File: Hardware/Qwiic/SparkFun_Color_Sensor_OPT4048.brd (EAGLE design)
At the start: 25.4 x 25.4 mm, 53 parts, among them J1 QWIIC_RIGHT_ANGLE, J2 QWIIC_RIGHT_ANGLE, U1 OPT4048

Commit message: Rolls version
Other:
- board text added: "v10"
- board text removed: "v01"
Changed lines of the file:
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@@
 <drawing>
 <settings>
-<setting alwaysvectorfont="no"/>
+<setting alwaysvectorfont="yes"/>
 <setting keepoldvectorfont="yes"/>
 <setting verticaltext="up"/>
@@
 <layer number="45" name="Holes" color="7" fill="1" visible="yes" active="yes"/>
 <layer number="46" name="Milling" color="3" fill="1" visible="no" active="yes"/>
-<layer number="47" name="Measures" color="7" fill="1" visible="no" active="yes"/>
+<layer number="47" name="Measures" color="7" fill="1" visible="yes" active="yes"/>
 <layer number="48" name="Document" color="7" fill="1" visible="no" active="yes"/>
 <layer number="49" name="Reference" color="13" fill="1" visible="yes" active="yes"/>
@@
 <wire x1="0" y1="0" x2="25.4" y2="0" width="0.2032" layer="20"/>
 <wire x1="25.4" y1="0" x2="25.4" y2="25.4" width="0.2032" layer="20"/>
-<text x="24.139525" y="11.420475" size="0.8128" layer="16" font="vector" ratio="22" rot="MR90">v01</text>
+<text x="24.139525" y="11.420475" size="0.8128" layer="16" font="vector" ratio="22" rot="MR90">v10</text>
 <text x="31.75" y="25.4" size="1.778" layer="51" font="vector">1.6mm Thickness
 1 oz. Copper
@@
 </signals>
 <mfgpreviewcolors>
-<mfgpreviewcolor name="soldermaskcolor" color="0xC8AA0000"/>
+<mfgpreviewcolor name="soldermaskcolor" color="0xC8000000"/>
 <mfgpreviewcolor name="silkscreencolor" color="0xFFFEFEFE"/>
-<mfgpreviewcolor name="backgroundcolor" color="0xFF282828"/>
+<mfgpreviewcolor name="backgroundcolor" color="0xFFFFFFFF"/>
 <mfgpreviewcolor name="coppercolor" color="0xFFFFBF00"/>
 <mfgpreviewcolor name="substratecolor" color="0xFF786E46"/>

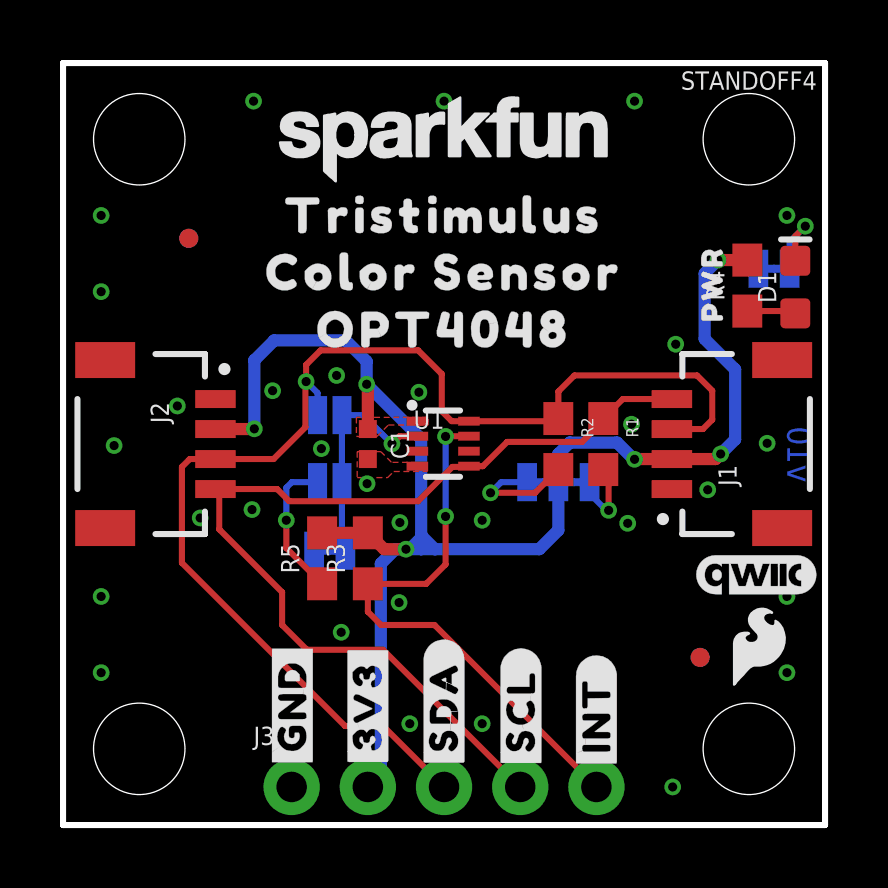
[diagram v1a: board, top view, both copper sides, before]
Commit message: Adds jumper to interrupt pin on both designs
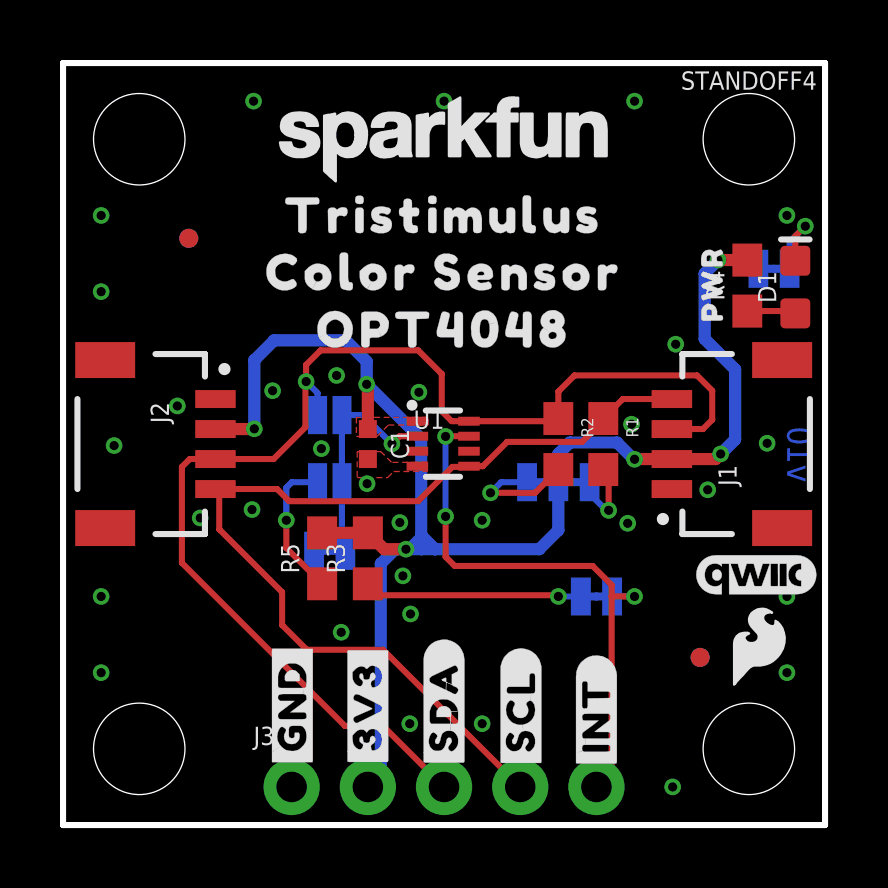
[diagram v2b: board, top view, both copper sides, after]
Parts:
- added INT: JUMPER-SMT_2_NC_TRACE_SILK, SparkFun-Jumpers:SMT-JUMPER_2_NC_TRACE_SILK
- added U$23: (no value), top:#INT#9
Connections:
- new net N$1: INT.2, R3.1
- net INT: now also INT.1; no longer R3.1
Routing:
- net N$1: track 0.00 -> 7.27 mm, vias 0 -> 1
- net INT: track 18.9 -> 19.2 mm, vias 2 -> 3
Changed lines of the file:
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@@
 <drawing>
 <settings>
-<setting alwaysvectorfont="yes"/>
+<setting alwaysvectorfont="no"/>
 <setting keepoldvectorfont="yes"/>
 <setting verticaltext="up"/>
@@
 <layer number="45" name="Holes" color="7" fill="1" visible="yes" active="yes"/>
 <layer number="46" name="Milling" color="3" fill="1" visible="no" active="yes"/>
-<layer number="47" name="Measures" color="7" fill="1" visible="yes" active="yes"/>
+<layer number="47" name="Measures" color="7" fill="1" visible="no" active="yes"/>
 <layer number="48" name="Document" color="7" fill="1" visible="no" active="yes"/>
 <layer number="49" name="Reference" color="13" fill="1" visible="yes" active="yes"/>
@@
 <element name="U$11" library="top" package="#0X45#18" value="" x="5.6896" y="11.4046" smashed="yes" rot="MR0"/>
 <element name="U$21" library="top" package="#0X46#18" value="" x="5.6388" y="13.589" smashed="yes" rot="MR0"/>
+<element name="INT" library="SparkFun-Jumpers" package="SMT-JUMPER_2_NC_TRACE_SILK" package3d_urn="urn:adsk.eagle:package:39281/1" value="JUMPER-SMT_2_NC_TRACE_SILK" x="17.78" y="7.62" smashed="yes" rot="MR0">
+<attribute name="NAME" x="17.78" y="8.763" size="0.6096" layer="26" font="vector" ratio="20" rot="MR0" align="bottom-center"/>
+<attribute name="VALUE" x="17.78" y="6.477" size="0.6096" layer="28" font="vector" ratio="20" rot="MR0" align="top-center"/>
+</element>
+<element name="U$23" library="top" package="#INT#9" value="" x="14.986" y="7.62" smashed="yes" rot="MR0"/>
 </elements>
 <signals>
@@
 <contactref element="J3" pad="1"/>
 <via x="11.2268" y="10.0838" extent="1-16" drill="0.3048"/>
-<via x="11.2014" y="7.4168" extent="1-16" drill="0.3048"/>
+<via x="11.5824" y="7.0358" extent="1-16" drill="0.3048"/>
 <via x="11.557" y="3.3782" extent="1-16" drill="0.3048"/>
 <via x="9.271" y="6.4262" extent="1-16" drill="0.3048"/>
@@
 <via x="9.1186" y="14.986" extent="1-16" drill="0.3048"/>
 <via x="8.6106" y="12.5476" extent="1-16" drill="0.3048"/>
+<via x="11.3284" y="8.3058" extent="1-16" drill="0.3048"/>
 </signal>
 <signal name="SCL">
@@
 <signal name="INT">
 <contactref element="U1" pad="P7"/>
-<contactref element="R3" pad="1"/>
 <wire x1="13.531" y1="12.962" x2="12.7588" y2="12.962" width="0.2032" layer="1"/>
 <wire x1="12.7588" y1="12.962" x2="12.7508" y2="12.954" width="0.2032" layer="1"/>
@@
 <wire x1="12.7508" y1="12.954" x2="12.7508" y2="10.287" width="0.2032" layer="16"/>
 <via x="12.7508" y="10.287" extent="1-16" drill="0.3048"/>
-<wire x1="10.16" y1="8.04" x2="12.104" y2="8.04" width="0.2032" layer="1"/>
-<wire x1="12.7508" y1="8.6868" x2="12.7508" y2="10.287" width="0.2032" layer="1"/>
-<wire x1="12.104" y1="8.04" x2="12.7508" y2="8.6868" width="0.2032" layer="1"/>
 <contactref element="J3" pad="5"/>
-<wire x1="17.78" y1="1.27" x2="12.381815625" y2="6.668184375" width="0.2032" layer="1"/>
-<wire x1="12.381815625" y1="6.668184375" x2="11.494184375" y2="6.668184375" width="0.2032" layer="1"/>
-<wire x1="11.494184375" y1="6.668184375" x2="10.603815625" y2="6.668184375" width="0.2032" layer="1"/>
-<wire x1="10.603815625" y1="6.668184375" x2="10.16" y2="7.112" width="0.2032" layer="1"/>
-<wire x1="10.16" y1="7.112" x2="10.16" y2="8.04" width="0.2032" layer="1"/>
+<contactref element="INT" pad="1"/>
+<wire x1="12.7508" y1="10.287" x2="12.7508" y2="8.9408" width="0.2032" layer="1"/>
+<wire x1="12.7508" y1="8.9408" x2="13.0556" y2="8.636" width="0.2032" layer="1"/>
+<wire x1="17.653" y1="8.636" x2="18.288" y2="8.001" width="0.2032" layer="1"/>
+<wire x1="18.288" y1="8.001" x2="18.288" y2="7.62" width="0.2032" layer="1"/>
+<wire x1="18.288" y1="7.62" x2="18.288" y2="1.778" width="0.2032" layer="1"/>
+<wire x1="18.288" y1="1.778" x2="17.78" y2="1.27" width="0.2032" layer="1"/>
+<wire x1="13.0556" y1="8.636" x2="17.653" y2="8.636" width="0.2032" layer="1"/>
+<wire x1="18.288" y1="7.62" x2="19.05" y2="7.62" width="0.2032" layer="1"/>
+<via x="19.05" y="7.62" extent="1-16" drill="0.3048"/>
+<wire x1="19.05" y1="7.62" x2="18.3007" y2="7.62" width="0.2032" layer="16"/>
 </signal>
 <signal name="3.3V">
@@
 <via x="7.4422" y="10.16" extent="1-16" drill="0.3048"/>
 </signal>
+<signal name="N$1">
+<contactref element="INT" pad="2"/>
+<contactref element="R3" pad="1"/>
+<wire x1="10.16" y1="8.04" x2="10.541" y2="7.659" width="0.2032" layer="1"/>
+<wire x1="16.471" y1="7.659" x2="10.541" y2="7.659" width="0.2032" layer="1"/>
+<wire x1="16.471" y1="7.659" x2="16.51" y2="7.62" width="0.2032" layer="1"/>
+<via x="16.51" y="7.62" extent="1-16" drill="0.3048"/>
+<wire x1="16.51" y1="7.62" x2="17.2593" y2="7.62" width="0.2032" layer="16"/>
+</signal>
 </signals>

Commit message: Revert "Adds jumper to interrupt pin on both designs"
This reverts commit a39334068ad88ec2875ce3e39fad74091b9d5839.
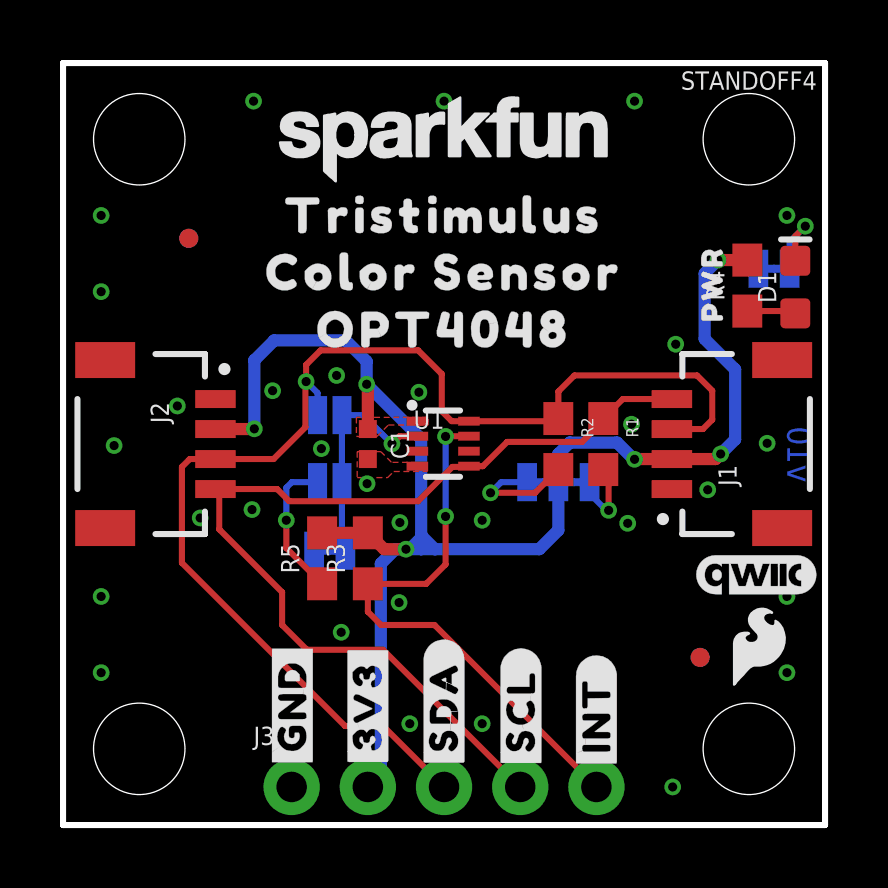
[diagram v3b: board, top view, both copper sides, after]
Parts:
- removed INT: JUMPER-SMT_2_NC_TRACE_SILK, SparkFun-Jumpers:SMT-JUMPER_2_NC_TRACE_SILK
- removed U$23: (no value), top:#INT#9
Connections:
- removed net N$1: INT.2, R3.1
- net INT: now also R3.1; no longer INT.1
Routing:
- net N$1: track 7.27 -> 0.00 mm, vias 1 -> 0
- net INT: track 19.2 -> 18.9 mm, vias 3 -> 2
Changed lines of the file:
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@@
 <drawing>
 <settings>
-<setting alwaysvectorfont="no"/>
+<setting alwaysvectorfont="yes"/>
 <setting keepoldvectorfont="yes"/>
 <setting verticaltext="up"/>
@@
 <layer number="45" name="Holes" color="7" fill="1" visible="yes" active="yes"/>
 <layer number="46" name="Milling" color="3" fill="1" visible="no" active="yes"/>
-<layer number="47" name="Measures" color="7" fill="1" visible="no" active="yes"/>
+<layer number="47" name="Measures" color="7" fill="1" visible="yes" active="yes"/>
 <layer number="48" name="Document" color="7" fill="1" visible="no" active="yes"/>
 <layer number="49" name="Reference" color="13" fill="1" visible="yes" active="yes"/>
@@
 <element name="U$11" library="top" package="#0X45#18" value="" x="5.6896" y="11.4046" smashed="yes" rot="MR0"/>
 <element name="U$21" library="top" package="#0X46#18" value="" x="5.6388" y="13.589" smashed="yes" rot="MR0"/>
-<element name="INT" library="SparkFun-Jumpers" package="SMT-JUMPER_2_NC_TRACE_SILK" package3d_urn="urn:adsk.eagle:package:39281/1" value="JUMPER-SMT_2_NC_TRACE_SILK" x="17.78" y="7.62" smashed="yes" rot="MR0">
-<attribute name="NAME" x="17.78" y="8.763" size="0.6096" layer="26" font="vector" ratio="20" rot="MR0" align="bottom-center"/>
-<attribute name="VALUE" x="17.78" y="6.477" size="0.6096" layer="28" font="vector" ratio="20" rot="MR0" align="top-center"/>
-</element>
-<element name="U$23" library="top" package="#INT#9" value="" x="14.986" y="7.62" smashed="yes" rot="MR0"/>
 </elements>
 <signals>
@@
 <contactref element="J3" pad="1"/>
 <via x="11.2268" y="10.0838" extent="1-16" drill="0.3048"/>
-<via x="11.5824" y="7.0358" extent="1-16" drill="0.3048"/>
+<via x="11.2014" y="7.4168" extent="1-16" drill="0.3048"/>
 <via x="11.557" y="3.3782" extent="1-16" drill="0.3048"/>
 <via x="9.271" y="6.4262" extent="1-16" drill="0.3048"/>
@@
 <via x="9.1186" y="14.986" extent="1-16" drill="0.3048"/>
 <via x="8.6106" y="12.5476" extent="1-16" drill="0.3048"/>
-<via x="11.3284" y="8.3058" extent="1-16" drill="0.3048"/>
 </signal>
 <signal name="SCL">
@@
 <signal name="INT">
 <contactref element="U1" pad="P7"/>
+<contactref element="R3" pad="1"/>
 <wire x1="13.531" y1="12.962" x2="12.7588" y2="12.962" width="0.2032" layer="1"/>
 <wire x1="12.7588" y1="12.962" x2="12.7508" y2="12.954" width="0.2032" layer="1"/>
@@
 <wire x1="12.7508" y1="12.954" x2="12.7508" y2="10.287" width="0.2032" layer="16"/>
 <via x="12.7508" y="10.287" extent="1-16" drill="0.3048"/>
+<wire x1="10.16" y1="8.04" x2="12.104" y2="8.04" width="0.2032" layer="1"/>
+<wire x1="12.7508" y1="8.6868" x2="12.7508" y2="10.287" width="0.2032" layer="1"/>
+<wire x1="12.104" y1="8.04" x2="12.7508" y2="8.6868" width="0.2032" layer="1"/>
 <contactref element="J3" pad="5"/>
-<contactref element="INT" pad="1"/>
-<wire x1="12.7508" y1="10.287" x2="12.7508" y2="8.9408" width="0.2032" layer="1"/>
-<wire x1="12.7508" y1="8.9408" x2="13.0556" y2="8.636" width="0.2032" layer="1"/>
-<wire x1="17.653" y1="8.636" x2="18.288" y2="8.001" width="0.2032" layer="1"/>
-<wire x1="18.288" y1="8.001" x2="18.288" y2="7.62" width="0.2032" layer="1"/>
-<wire x1="18.288" y1="7.62" x2="18.288" y2="1.778" width="0.2032" layer="1"/>
-<wire x1="18.288" y1="1.778" x2="17.78" y2="1.27" width="0.2032" layer="1"/>
-<wire x1="13.0556" y1="8.636" x2="17.653" y2="8.636" width="0.2032" layer="1"/>
-<wire x1="18.288" y1="7.62" x2="19.05" y2="7.62" width="0.2032" layer="1"/>
-<via x="19.05" y="7.62" extent="1-16" drill="0.3048"/>
-<wire x1="19.05" y1="7.62" x2="18.3007" y2="7.62" width="0.2032" layer="16"/>
+<wire x1="17.78" y1="1.27" x2="12.381815625" y2="6.668184375" width="0.2032" layer="1"/>
+<wire x1="12.381815625" y1="6.668184375" x2="11.494184375" y2="6.668184375" width="0.2032" layer="1"/>
+<wire x1="11.494184375" y1="6.668184375" x2="10.603815625" y2="6.668184375" width="0.2032" layer="1"/>
+<wire x1="10.603815625" y1="6.668184375" x2="10.16" y2="7.112" width="0.2032" layer="1"/>
+<wire x1="10.16" y1="7.112" x2="10.16" y2="8.04" width="0.2032" layer="1"/>
 </signal>
 <signal name="3.3V">
@@
 <via x="7.4422" y="10.16" extent="1-16" drill="0.3048"/>
 </signal>
-<signal name="N$1">
-<contactref element="INT" pad="2"/>
-<contactref element="R3" pad="1"/>
-<wire x1="10.16" y1="8.04" x2="10.541" y2="7.659" width="0.2032" layer="1"/>
-<wire x1="16.471" y1="7.659" x2="10.541" y2="7.659" width="0.2032" layer="1"/>
-<wire x1="16.471" y1="7.659" x2="16.51" y2="7.62" width="0.2032" layer="1"/>
-<via x="16.51" y="7.62" extent="1-16" drill="0.3048"/>
-<wire x1="16.51" y1="7.62" x2="17.2593" y2="7.62" width="0.2032" layer="16"/>
-</signal>
 </signals>

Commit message: Adds second Qwiic label, spins version number
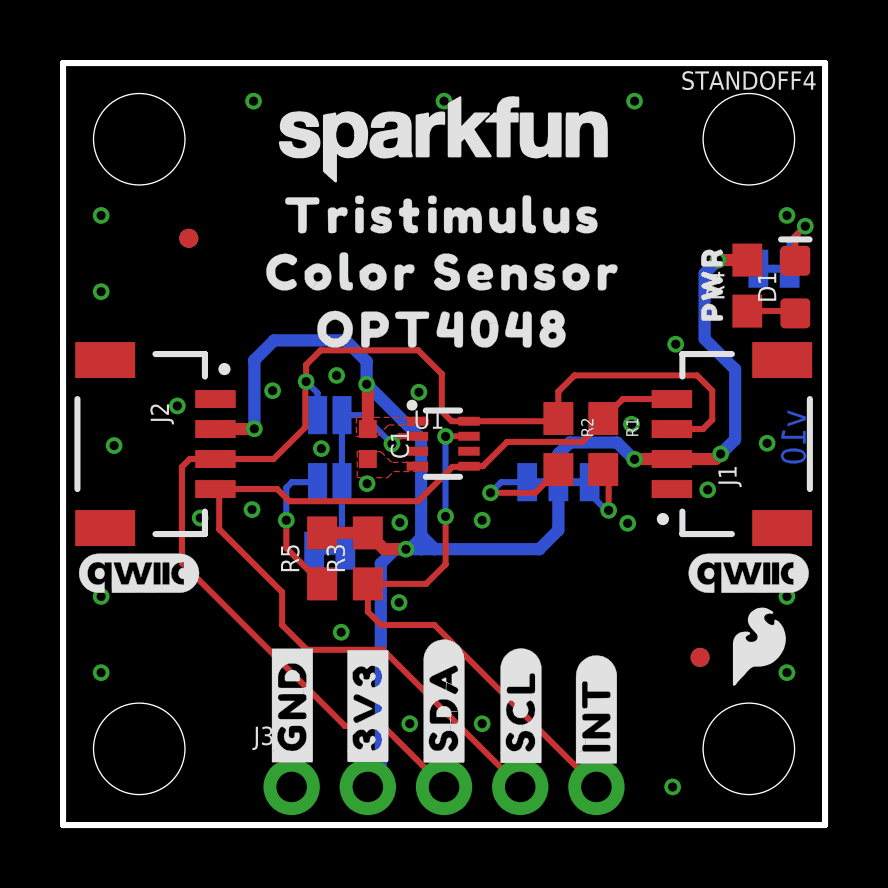
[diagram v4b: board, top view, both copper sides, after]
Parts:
- added LOGO5: QWIIC_LOGO_4MM, SparkFun-Aesthetics:QWIIC_4MM
- moved LOGO1 0.26 mm to (22.9, 8.38)
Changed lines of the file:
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@@
 <drawing>
 <settings>
-<setting alwaysvectorfont="yes"/>
+<setting alwaysvectorfont="no"/>
 <setting keepoldvectorfont="yes"/>
 <setting verticaltext="up"/>
@@
 <layer number="45" name="Holes" color="7" fill="1" visible="yes" active="yes"/>
 <layer number="46" name="Milling" color="3" fill="1" visible="no" active="yes"/>
-<layer number="47" name="Measures" color="7" fill="1" visible="yes" active="yes"/>
+<layer number="47" name="Measures" color="7" fill="1" visible="no" active="yes"/>
 <layer number="48" name="Document" color="7" fill="1" visible="no" active="yes"/>
 <layer number="49" name="Reference" color="13" fill="1" visible="yes" active="yes"/>
@@
 <wire x1="0" y1="0" x2="25.4" y2="0" width="0.2032" layer="20"/>
 <wire x1="25.4" y1="0" x2="25.4" y2="25.4" width="0.2032" layer="20"/>
-<text x="24.139525" y="11.420475" size="0.8128" layer="16" font="vector" ratio="22" rot="MR90">v10</text>
+<text x="24.755475" y="13.852525" size="0.8128" layer="16" font="vector" ratio="22" rot="SMR270">v10</text>
 <text x="31.75" y="25.4" size="1.778" layer="51" font="vector">1.6mm Thickness
 1 oz. Copper
@@
 <element name="FD1" library="SparkFun-Aesthetics" package="FIDUCIAL-MICRO" value="FIDUCIALUFIDUCIAL" x="4.191" y="19.558" smashed="yes" rot="MR0"/>
 <element name="FD2" library="SparkFun-Aesthetics" package="FIDUCIAL-MICRO" value="FIDUCIALUFIDUCIAL" x="21.2344" y="5.588" smashed="yes" rot="MR0"/>
-<element name="LOGO1" library="SparkFun-Aesthetics" package="QWIIC_4MM" value="QWIIC_LOGO_4MM" x="23.114" y="8.3312" smashed="yes"/>
+<element name="LOGO1" library="SparkFun-Aesthetics" package="QWIIC_4MM" value="QWIIC_LOGO_4MM" x="22.86" y="8.382" smashed="yes"/>
 <element name="U$1" library="top" package="#3V3#1" value="" x="10.16" y="3.9624" smashed="yes" rot="R90"/>
 <element name="U$2" library="top" package="#GND#0" value="" x="7.6454" y="3.9878" smashed="yes" rot="R90"/>
@@
 <element name="U$11" library="top" package="#0X45#18" value="" x="5.6896" y="11.4046" smashed="yes" rot="MR0"/>
 <element name="U$21" library="top" package="#0X46#18" value="" x="5.6388" y="13.589" smashed="yes" rot="MR0"/>
+<element name="LOGO5" library="SparkFun-Aesthetics" package="QWIIC_4MM" value="QWIIC_LOGO_4MM" x="2.54" y="8.382" smashed="yes"/>
 </elements>
 <signals>
